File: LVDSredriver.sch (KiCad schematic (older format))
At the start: 8 parts, among them U2 DS90LV004

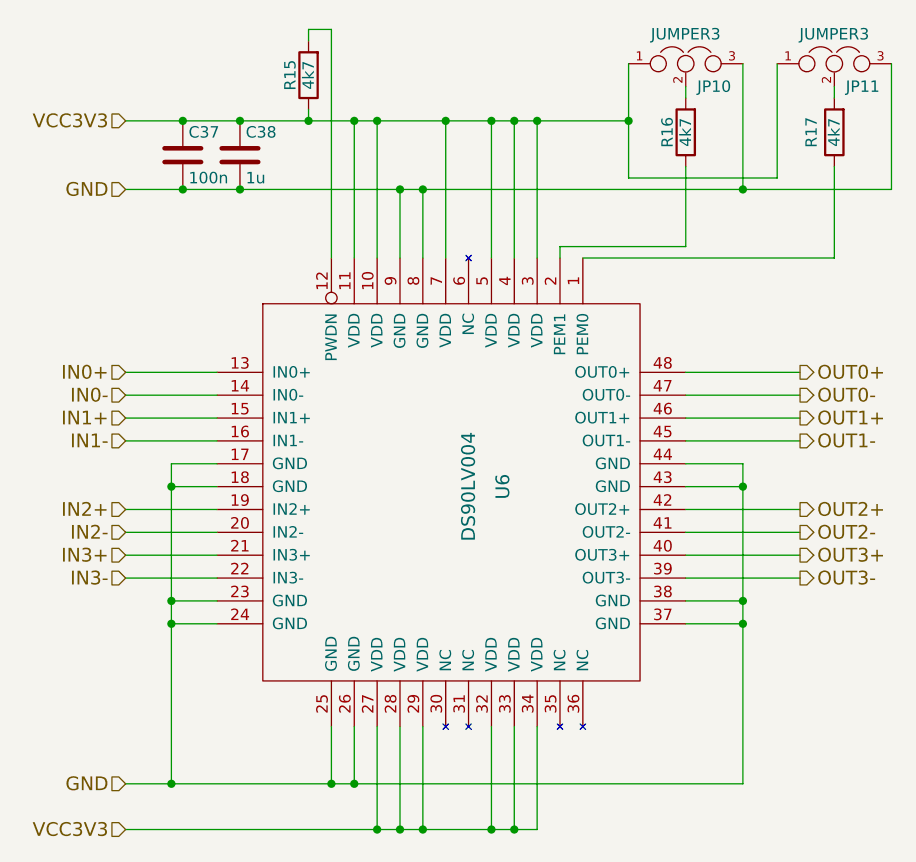
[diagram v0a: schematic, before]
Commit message: Route power, reroute data signals to top layer
Signed-off-by: katie dunne <kedunne@lbl.gov>
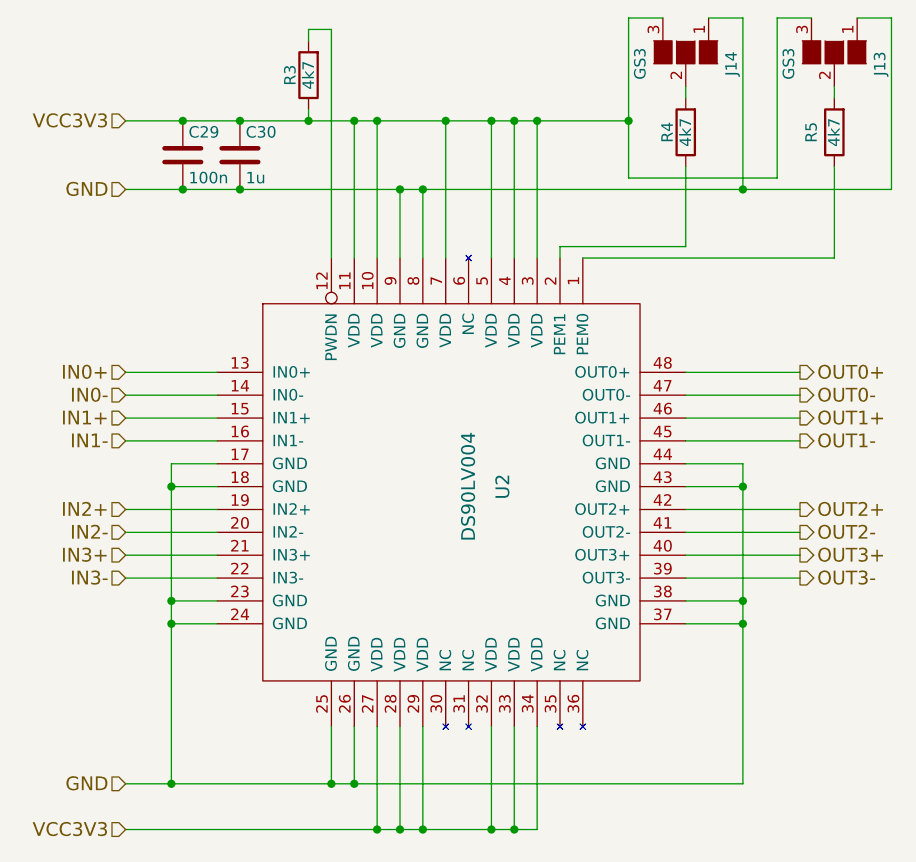
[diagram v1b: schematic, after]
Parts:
- removed JP2, JP3: JUMPER3, Connectors:GS3, symbol JUMPER3
- added J14, J15: GS3, Connectors:GS3, symbol GS3
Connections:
- net GND: now also J14.1 (G1), J15.1 (G1)
- net VCC3V3: now also J14.3 (G3), J15.3 (G3)
- net at R5.2: now also J15.2 (G2)
- net at R4.2: now also J14.2 (G2)
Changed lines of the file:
@@
 EESchema Schematic File Version 2
+LIBS:vhdci_fei4_rj45-rescue
+LIBS:ds90lv004
+LIBS:con-molex-vhdci
 LIBS:power
 LIBS:device
@@
 AR Path="/590F7135/590C994A" Ref="U6"  Part="1"
 AR Path="/590FA61B/590C994A" Ref="U7"  Part="1"
-F 0 "U6" H 5100 3250 60  0000 C CNN
+F 0 "U2" H 5100 3250 60  0000 C CNN
 F 1 "DS90LV004" H 5100 3100 60  0000 C CNN
 F 2 "Housings_QFP:TQFP-48_7x7mm_Pitch0.5mm" H 4300 2200 60  0001 C CNN
@@
 AR Path="/590F7135/590C9D1C" Ref="C37"  Part="1"
 AR Path="/590FA61B/590C9D1C" Ref="C39"  Part="1"
-F 0 "C37" H 3975 1650 50  0000 L CNN
+F 0 "C29" H 3975 1650 50  0000 L CNN
 F 1 "100n" H 3975 1450 50  0000 L CNN
 F 2 "Capacitors_SMD:C_0805_HandSoldering" H 3988 1400 50  0001 C CNN
@@
 AR Path="/590F7135/590C9D42" Ref="C38"  Part="1"
 AR Path="/590FA61B/590C9D42" Ref="C40"  Part="1"
-F 0 "C38" H 4225 1650 50  0000 L CNN
+F 0 "C30" H 4225 1650 50  0000 L CNN
 F 1 "1u" H 4225 1450 50  0000 L CNN
 F 2 "Capacitors_SMD:C_0805_HandSoldering" H 4238 1400 50  0001 C CNN
@@
 Connection ~ 5300 1400
 Wire Wire Line
-	3700 1700 7050 1700
+	7050 1700 3700 1700
 Connection ~ 3950 1700
 Wire Wire Line
@@
 AR Path="/590F7135/590CAD65" Ref="R17"  Part="1"
 AR Path="/590FA61B/590CAD65" Ref="R20"  Part="1"
-F 0 "R17" V 6900 1450 50  0000 C CNN
+F 0 "R5" V 6900 1450 50  0000 C CNN
 F 1 "4k7" V 6800 1450 50  0000 C CNN
 F 2 "Resistors_SMD:R_0603_HandSoldering" V 6730 1450 50  0001 C CNN
@@
 AR Path="/590F7135/590CAE08" Ref="R16"  Part="1"
 AR Path="/590FA61B/590CAE08" Ref="R19"  Part="1"
-F 0 "R16" V 6230 1450 50  0000 C CNN
+F 0 "R4" V 6230 1450 50  0000 C CNN
 F 1 "4k7" V 6150 1450 50  0000 C CNN
 F 2 "Resistors_SMD:R_0603_HandSoldering" V 6080 1450 50  0001 C CNN
@@
 Text HLabel 3700 1700 0    60   Input ~ 0
 GND
-$Comp
-L JUMPER3 JP2
-U 1 1 590E234E
-P 6150 1150
-AR Path="/590C98D3/590E234E" Ref="JP2"  Part="1"
-AR Path="/590CDB7D/590E234E" Ref="JP4"  Part="1"
-AR Path="/590D211A/590E234E" Ref="JP6"  Part="1"
-AR Path="/590D50A0/590E234E" Ref="JP8"  Part="1"
-AR Path="/590F7135/590E234E" Ref="JP10"  Part="1"
-AR Path="/590FA61B/590E234E" Ref="JP12"  Part="1"
-F 0 "JP10" H 6200 1050 50  0000 L CNN
-F 1 "JUMPER3" H 6150 1250 50  0000 C BNN
-F 2 "Connectors:GS3" H 6150 1150 50  0001 C CNN
-F 3 "" H 6150 1150 50  0000 C CNN
-	1    6150 1150
-	1    0    0    -1
-$EndComp
-$Comp
-L JUMPER3 JP3
-U 1 1 590E238E
-P 6800 1150
-AR Path="/590C98D3/590E238E" Ref="JP3"  Part="1"
-AR Path="/590CDB7D/590E238E" Ref="JP5"  Part="1"
-AR Path="/590D211A/590E238E" Ref="JP7"  Part="1"
-AR Path="/590D50A0/590E238E" Ref="JP9"  Part="1"
-AR Path="/590F7135/590E238E" Ref="JP11"  Part="1"
-AR Path="/590FA61B/590E238E" Ref="JP13"  Part="1"
-F 0 "JP11" H 6850 1050 50  0000 L CNN
-F 1 "JUMPER3" H 6800 1250 50  0000 C BNN
-F 2 "Connectors:GS3" H 6800 1150 50  0001 C CNN
-F 3 "" H 6800 1150 50  0000 C CNN
-	1    6800 1150
-	1    0    0    -1
-$EndComp
 Wire Wire Line
 	6150 1950 6150 1600
@@
 	6800 2000 6800 1600
 Wire Wire Line
-	6400 1700 6400 1150
-Wire Wire Line
-	7050 1700 7050 1150
+	6400 950  6400 1700
+Wire Wire Line
+	7050 950  7050 1700
 Connection ~ 6400 1700
 Wire Wire Line
-	5900 1150 5900 1650
+	5900 950  5900 1650
 Wire Wire Line
 	5900 1650 6550 1650
 Wire Wire Line
-	6550 1650 6550 1150
+	6550 1650 6550 950
 Connection ~ 5900 1400
 $Comp
@@
 AR Path="/590F7135/590FDA86" Ref="R15"  Part="1"
 AR Path="/590FA61B/590FDA86" Ref="R18"  Part="1"
-F 0 "R15" V 4580 1200 50  0000 C CNN
+F 0 "R3" V 4580 1200 50  0000 C CNN
 F 1 "4k7" V 4500 1200 50  0000 C CNN
 F 2 "Resistors_SMD:R_0603_HandSoldering" V 4430 1200 50  0001 C CNN
@@
 Wire Wire Line
 	6800 1300 6800 1250
+$Comp
+L GS3 J15
+U 1 1 59160514
+P 6800 1100
+AR Path="/590CDB7D/59160514" Ref="J15"  Part="1"
+AR Path="/590C98D3/59160514" Ref="J13"  Part="1"
+AR Path="/590D211A/59160514" Ref="J17"  Part="1"
+AR Path="/590D50A0/59160514" Ref="J19"  Part="1"
+AR Path="/590F7135/59160514" Ref="J21"  Part="1"
+AR Path="/590FA61B/59160514" Ref="J23"  Part="1"
+F 0 "J13" H 6850 1300 50  0000 C CNN
+F 1 "GS3" H 6850 901 50  0000 C CNN
+F 2 "Connectors:GS3" V 6888 1026 50  0001 C CNN
+F 3 "" H 6800 1100 50  0001 C CNN
+	1    6800 1100
+	0    1    1    0
+$EndComp
+Wire Wire Line
+	6550 950  6700 950
+Wire Wire Line
+	6400 950  6250 950
+Wire Wire Line
+	5900 950  6050 950
+Wire Wire Line
+	6900 950  7050 950
+$Comp
+L GS3 J14
+U 1 1 59174CD2
+P 6150 1100
+AR Path="/590C98D3/59174CD2" Ref="J14"  Part="1"
+AR Path="/590CDB7D/59174CD2" Ref="J16"  Part="1"
+AR Path="/590D211A/59174CD2" Ref="J18"  Part="1"
+AR Path="/590D50A0/59174CD2" Ref="J20"  Part="1"
+AR Path="/590F7135/59174CD2" Ref="J22"  Part="1"
+AR Path="/590FA61B/59174CD2" Ref="J25"  Part="1"
+F 0 "J14" H 6200 1300 50  0000 C CNN
+F 1 "GS3" H 6200 901 50  0000 C CNN
+F 2 "Connectors:GS3" V 6238 1026 50  0001 C CNN
+F 3 "" H 6150 1100 50  0001 C CNN
+	1    6150 1100
+	0    1    1    0
+$EndComp
 $EndSCHEMATC

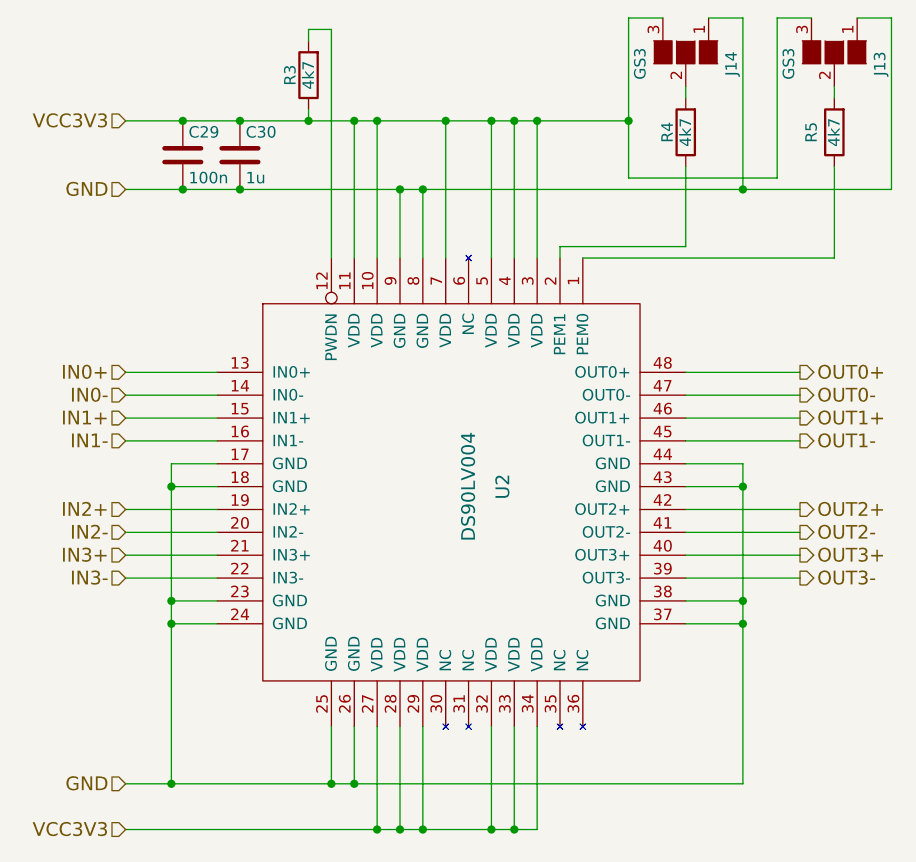
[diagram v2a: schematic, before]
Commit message: Route 2 level shifters
Signed-off-by: katie dunne <kedunne@lbl.gov>
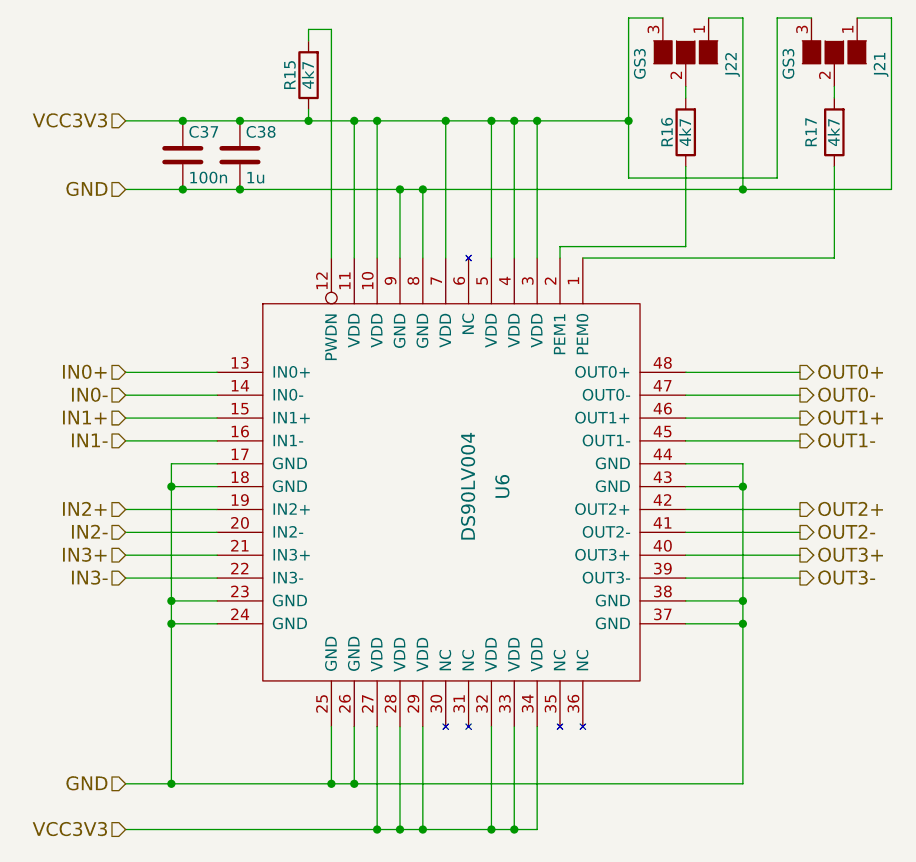
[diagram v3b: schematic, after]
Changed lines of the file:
@@
 EESchema Schematic File Version 2
 LIBS:vhdci_fei4_rj45-rescue
+LIBS:ds90lv004
+LIBS:con-molex-vhdci
 LIBS:power
 LIBS:device
@@
 LIBS:contrib
 LIBS:valves
+LIBS:module
 LIBS:vhdci_fei4_rj45-cache
 EELAYER 25 0
@@
 $Descr A4 11693 8268
 encoding utf-8
-Sheet 2 10
+Sheet 6 10
 Title "VHDCI FE-I4 RJ45 Adapter"
 Date "2017-05-05"
@@
 AR Path="/590F7135/590C994A" Ref="U6"  Part="1"
 AR Path="/590FA61B/590C994A" Ref="U7"  Part="1"
-F 0 "U2" H 5100 3250 60  0000 C CNN
+F 0 "U6" H 5100 3250 60  0000 C CNN
 F 1 "DS90LV004" H 5100 3100 60  0000 C CNN
 F 2 "Housings_QFP:TQFP-48_7x7mm_Pitch0.5mm" H 4300 2200 60  0001 C CNN
@@
 AR Path="/590F7135/590C9D1C" Ref="C37"  Part="1"
 AR Path="/590FA61B/590C9D1C" Ref="C39"  Part="1"
-F 0 "C29" H 3975 1650 50  0000 L CNN
+F 0 "C37" H 3975 1650 50  0000 L CNN
 F 1 "100n" H 3975 1450 50  0000 L CNN
 F 2 "Capacitors_SMD:C_0805_HandSoldering" H 3988 1400 50  0001 C CNN
@@
 AR Path="/590F7135/590C9D42" Ref="C38"  Part="1"
 AR Path="/590FA61B/590C9D42" Ref="C40"  Part="1"
-F 0 "C30" H 4225 1650 50  0000 L CNN
+F 0 "C38" H 4225 1650 50  0000 L CNN
 F 1 "1u" H 4225 1450 50  0000 L CNN
 F 2 "Capacitors_SMD:C_0805_HandSoldering" H 4238 1400 50  0001 C CNN
@@
 AR Path="/590F7135/590CAD65" Ref="R17"  Part="1"
 AR Path="/590FA61B/590CAD65" Ref="R20"  Part="1"
-F 0 "R5" V 6900 1450 50  0000 C CNN
+F 0 "R17" V 6900 1450 50  0000 C CNN
 F 1 "4k7" V 6800 1450 50  0000 C CNN
 F 2 "Resistors_SMD:R_0603_HandSoldering" V 6730 1450 50  0001 C CNN
@@
 AR Path="/590F7135/590CAE08" Ref="R16"  Part="1"
 AR Path="/590FA61B/590CAE08" Ref="R19"  Part="1"
-F 0 "R4" V 6230 1450 50  0000 C CNN
+F 0 "R16" V 6230 1450 50  0000 C CNN
 F 1 "4k7" V 6150 1450 50  0000 C CNN
 F 2 "Resistors_SMD:R_0603_HandSoldering" V 6080 1450 50  0001 C CNN
@@
 AR Path="/590F7135/590FDA86" Ref="R15"  Part="1"
 AR Path="/590FA61B/590FDA86" Ref="R18"  Part="1"
-F 0 "R3" V 4580 1200 50  0000 C CNN
+F 0 "R15" V 4580 1200 50  0000 C CNN
 F 1 "4k7" V 4500 1200 50  0000 C CNN
 F 2 "Resistors_SMD:R_0603_HandSoldering" V 4430 1200 50  0001 C CNN
@@
 AR Path="/590F7135/59160514" Ref="J21"  Part="1"
 AR Path="/590FA61B/59160514" Ref="J23"  Part="1"
-F 0 "J13" H 6850 1300 50  0000 C CNN
+F 0 "J21" H 6850 1300 50  0000 C CNN
 F 1 "GS3" H 6850 901 50  0000 C CNN
 F 2 "Connectors:GS3" V 6888 1026 50  0001 C CNN
@@
 AR Path="/590F7135/59174CD2" Ref="J22"  Part="1"
 AR Path="/590FA61B/59174CD2" Ref="J25"  Part="1"
-F 0 "J14" H 6200 1300 50  0000 C CNN
+F 0 "J22" H 6200 1300 50  0000 C CNN
 F 1 "GS3" H 6200 901 50  0000 C CNN
 F 2 "Connectors:GS3" V 6238 1026 50  0001 C CNN
